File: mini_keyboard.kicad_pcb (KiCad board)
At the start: 2 copper layers, 61 x 53.3 mm, 2 parts, among them SW1 SW_DIP_x01, U1 ARDUINO_MICRO_SHIELD

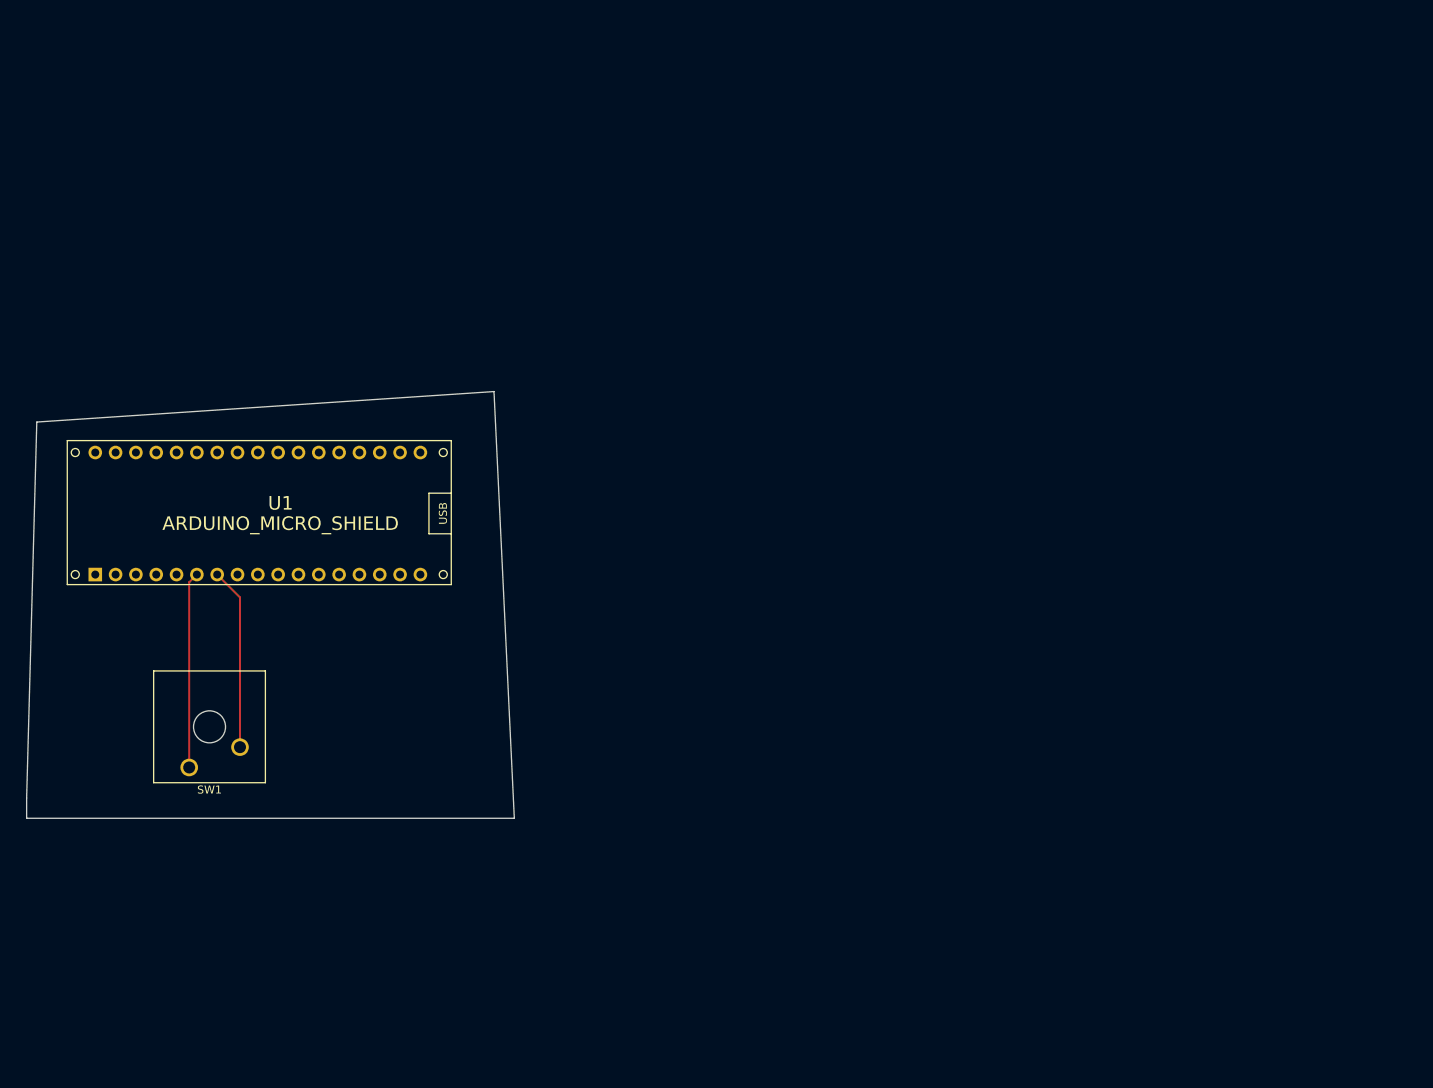
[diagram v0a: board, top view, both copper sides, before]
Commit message: PCB ready, no cables
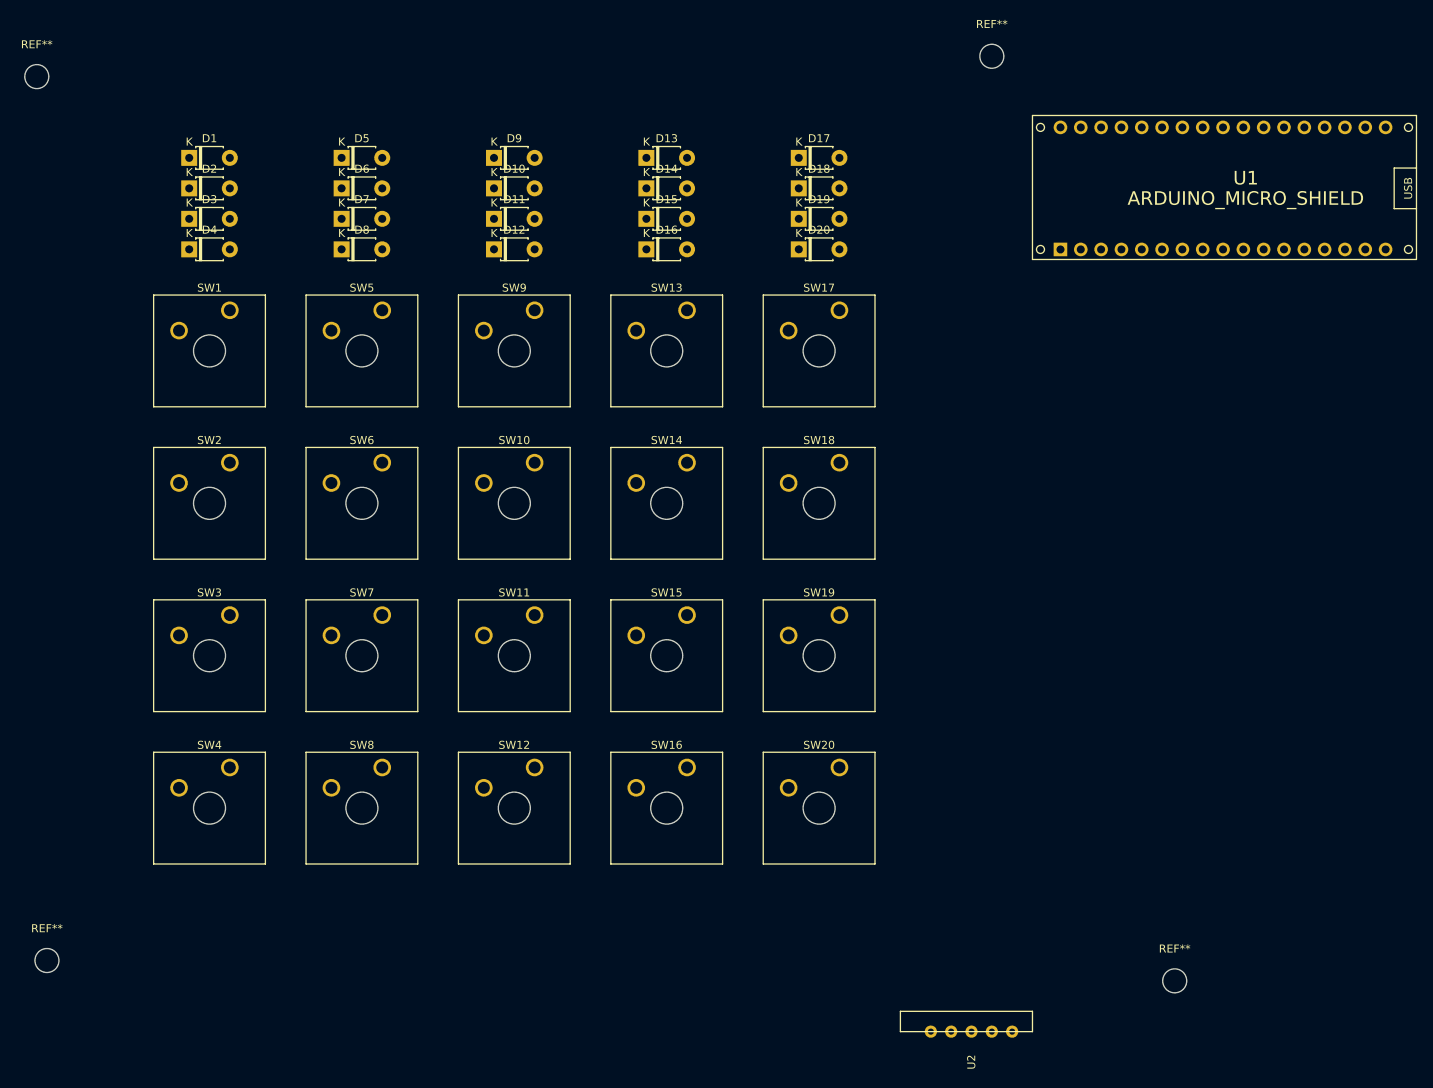
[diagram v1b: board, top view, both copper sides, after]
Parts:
- added D1: DIODE, Diode_THT:D_T-1_P5.08mm_Horizontal, F.Cu at (100.3, 33.0)
- added D10: DIODE, Diode_THT:D_T-1_P5.08mm_Horizontal, F.Cu at (138.4, 36.8)
- added D11: DIODE, Diode_THT:D_T-1_P5.08mm_Horizontal, F.Cu at (138.4, 40.6)
- added D12: DIODE, Diode_THT:D_T-1_P5.08mm_Horizontal, F.Cu at (138.4, 44.5)
- added D13: DIODE, Diode_THT:D_T-1_P5.08mm_Horizontal, F.Cu at (157.5, 33.0)
- added D14: DIODE, Diode_THT:D_T-1_P5.08mm_Horizontal, F.Cu at (157.5, 36.8)
- added D15: DIODE, Diode_THT:D_T-1_P5.08mm_Horizontal, F.Cu at (157.5, 40.6)
- added D16: DIODE, Diode_THT:D_T-1_P5.08mm_Horizontal, F.Cu at (157.5, 44.5)
- added D17: DIODE, Diode_THT:D_T-1_P5.08mm_Horizontal, F.Cu at (176.5, 33.0)
- added D18: DIODE, Diode_THT:D_T-1_P5.08mm_Horizontal, F.Cu at (176.5, 36.8)
- added D19: DIODE, Diode_THT:D_T-1_P5.08mm_Horizontal, F.Cu at (176.5, 40.6)
- added D2: DIODE, Diode_THT:D_T-1_P5.08mm_Horizontal, F.Cu at (100.3, 36.8)
- added D20: DIODE, Diode_THT:D_T-1_P5.08mm_Horizontal, F.Cu at (176.5, 44.5)
- added D3: DIODE, Diode_THT:D_T-1_P5.08mm_Horizontal, F.Cu at (100.3, 40.6)
- added D4: DIODE, Diode_THT:D_T-1_P5.08mm_Horizontal, F.Cu at (100.3, 44.5)
- added D5: DIODE, Diode_THT:D_T-1_P5.08mm_Horizontal, F.Cu at (119.4, 33.0)
- added D6: DIODE, Diode_THT:D_T-1_P5.08mm_Horizontal, F.Cu at (119.4, 36.8)
- added D7: DIODE, Diode_THT:D_T-1_P5.08mm_Horizontal, F.Cu at (119.4, 40.6)
- added D8: DIODE, Diode_THT:D_T-1_P5.08mm_Horizontal, F.Cu at (119.4, 44.5)
- added D9: DIODE, Diode_THT:D_T-1_P5.08mm_Horizontal, F.Cu at (138.4, 33.0)
- added REF**: MountingHole_3mm, MountingHole:MountingHole_3mm, F.Cu at (81.3, 22.9)
- added REF**: MountingHole_3mm, MountingHole:MountingHole_3mm, F.Cu at (200.7, 20.3)
- added REF**: MountingHole_3mm, MountingHole:MountingHole_3mm, F.Cu at (223.5, 135.9)
- added REF**: MountingHole_3mm, MountingHole:MountingHole_3mm, F.Cu at (82.5, 133.3)
- added SW10: SW_DIP_x01, Button_Switch_Keyboard:SW_Cherry_MX_1.00u_Plate, F.Cu at (143.5, 71.1)
- added SW11: SW_DIP_x01, Button_Switch_Keyboard:SW_Cherry_MX_1.00u_Plate, F.Cu at (143.5, 90.2)
- added SW12: SW_DIP_x01, Button_Switch_Keyboard:SW_Cherry_MX_1.00u_Plate, F.Cu at (143.5, 109.2)
- added SW13: SW_DIP_x01, Button_Switch_Keyboard:SW_Cherry_MX_1.00u_Plate, F.Cu at (162.6, 52.1)
- added SW14: SW_DIP_x01, Button_Switch_Keyboard:SW_Cherry_MX_1.00u_Plate, F.Cu at (162.6, 71.1)
- added SW15: SW_DIP_x01, Button_Switch_Keyboard:SW_Cherry_MX_1.00u_Plate, F.Cu at (162.6, 90.2)
- added SW16: SW_DIP_x01, Button_Switch_Keyboard:SW_Cherry_MX_1.00u_Plate, F.Cu at (162.6, 109.2)
- added SW17: SW_DIP_x01, Button_Switch_Keyboard:SW_Cherry_MX_1.00u_Plate, F.Cu at (181.6, 52.1)
- added SW18: SW_DIP_x01, Button_Switch_Keyboard:SW_Cherry_MX_1.00u_Plate, F.Cu at (181.6, 71.1)
- added SW19: SW_DIP_x01, Button_Switch_Keyboard:SW_Cherry_MX_1.00u_Plate, F.Cu at (181.6, 90.2)
- added SW2: SW_DIP_x01, Button_Switch_Keyboard:SW_Cherry_MX_1.00u_Plate, F.Cu at (105.4, 71.1)
- added SW20: SW_DIP_x01, Button_Switch_Keyboard:SW_Cherry_MX_1.00u_Plate, F.Cu at (181.6, 109.2)
- added SW3: SW_DIP_x01, Button_Switch_Keyboard:SW_Cherry_MX_1.00u_Plate, F.Cu at (105.4, 90.2)
- added SW4: SW_DIP_x01, Button_Switch_Keyboard:SW_Cherry_MX_1.00u_Plate, F.Cu at (105.4, 109.2)
- added SW5: SW_DIP_x01, Button_Switch_Keyboard:SW_Cherry_MX_1.00u_Plate, F.Cu at (124.5, 52.1)
- added SW6: SW_DIP_x01, Button_Switch_Keyboard:SW_Cherry_MX_1.00u_Plate, F.Cu at (124.5, 71.1)
- added SW7: SW_DIP_x01, Button_Switch_Keyboard:SW_Cherry_MX_1.00u_Plate, F.Cu at (124.5, 90.2)
- added SW8: SW_DIP_x01, Button_Switch_Keyboard:SW_Cherry_MX_1.00u_Plate, F.Cu at (124.5, 109.2)
- added SW9: SW_DIP_x01, Button_Switch_Keyboard:SW_Cherry_MX_1.00u_Plate, F.Cu at (143.5, 52.1)
- added U2: Joystick, Joystick:Joystick, F.Cu at (203.2, 142.2)
- moved U1 127.3 mm to (205.7, 45.7)
- moved SW1 57.4 mm to (105.4, 52.1), turned to 0 degrees
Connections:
- SW1 pad 1: Net-(SW1-Pad1) -> Net-(D1-Pad2)
- U1 pad 2: Net-(SW1-Pad2) -> Net-(D1-Pad1)
- U1 pad A5: Net-(U1-PadA5) -> Net-(SW1-Pad2)
- U1 pad GND: Net-(SW1-Pad1) -> Net-(U1-PadGND)
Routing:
- net Net-(SW1-Pad1): track 24.5 -> 0.00 mm
- net Net-(SW1-Pad2): track 22.8 -> 0.00 mm
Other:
- board outline removed

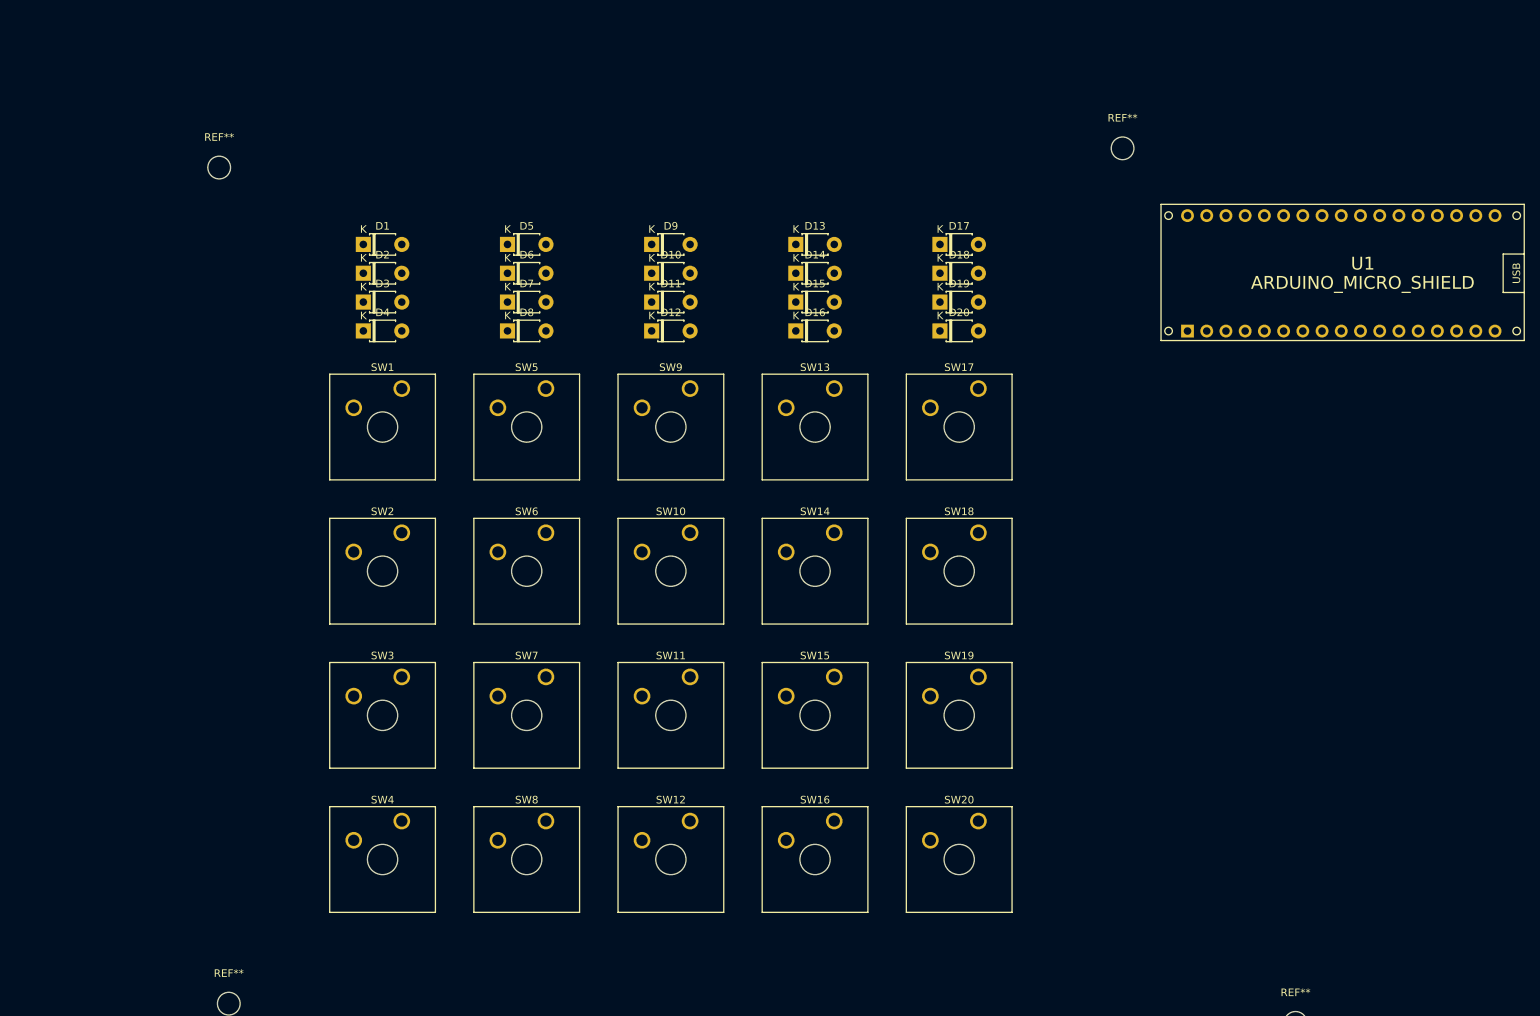
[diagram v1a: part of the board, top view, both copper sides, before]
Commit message: Moved buttons and made some lines
Problem: Some cables are crossing
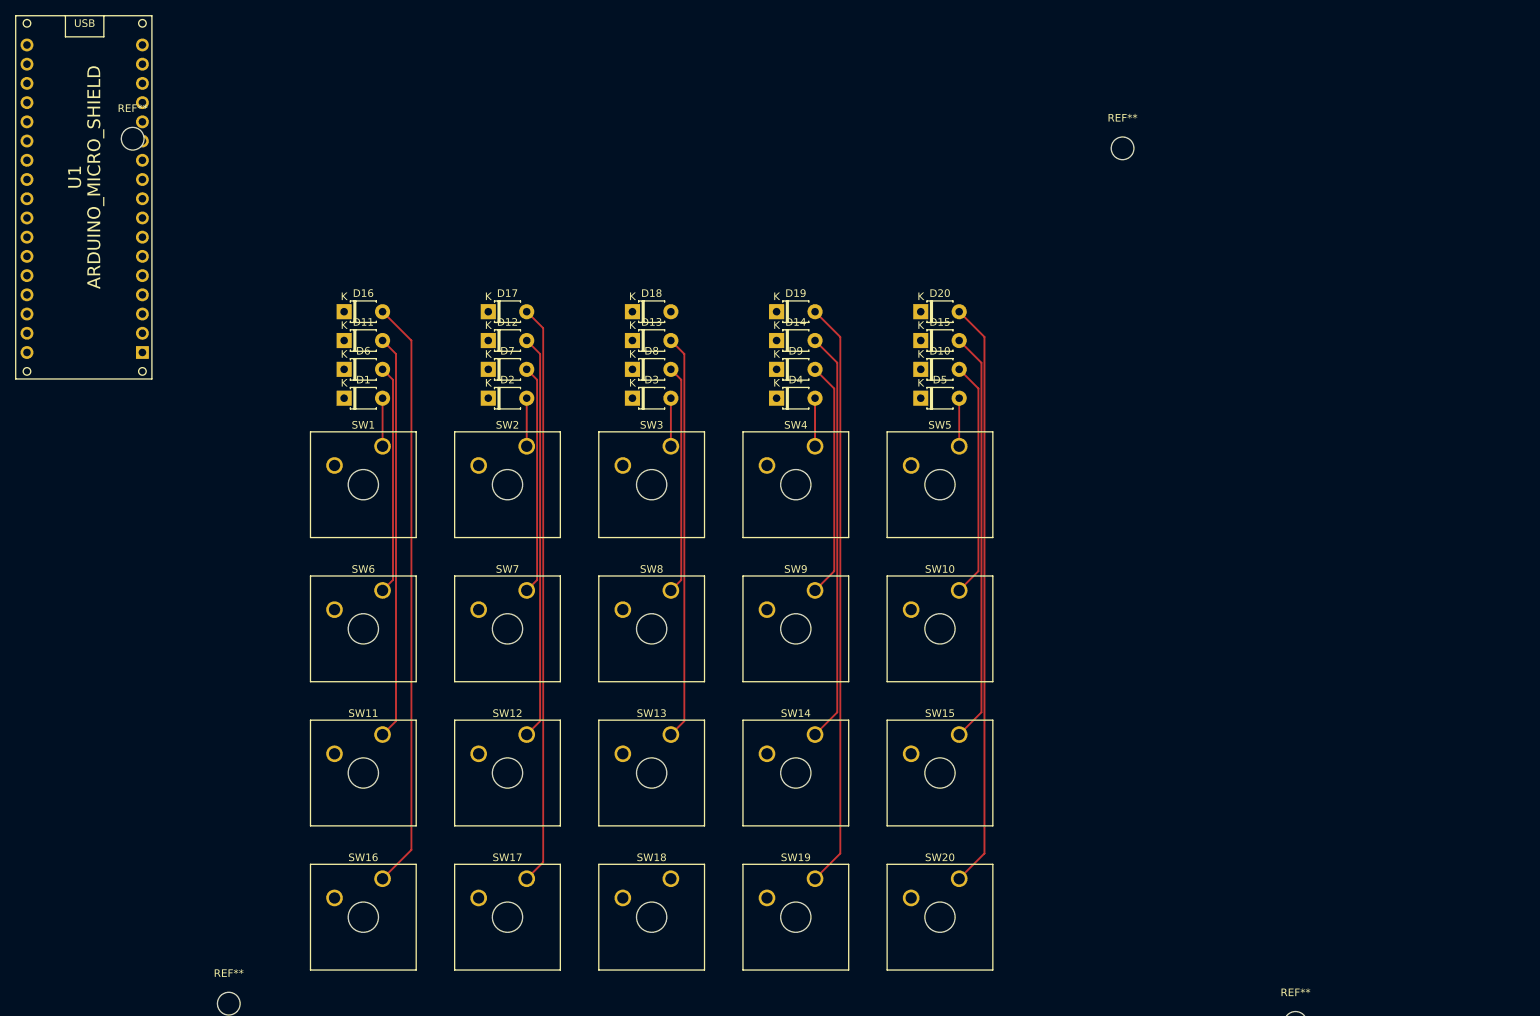
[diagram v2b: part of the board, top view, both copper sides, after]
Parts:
- moved U1 133.4 mm to (72.4, 50.8), turned to 90 degrees
- moved SW17 88.1 mm to (121.9, 116.8)
- moved SW4 73.7 mm to (160.0, 59.7)
- moved SW18 61.2 mm to (141.0, 116.8)
- moved D17 60.3 mm to (116.8, 41.9)
- moved SW16 60.2 mm to (102.9, 116.8)
- moved D16 59.7 mm to (97.8, 41.9)
- moved D5 58.3 mm to (174.0, 53.3)
- moved D4 55.3 mm to (154.9, 53.3)
- moved SW5 55.1 mm to (179.1, 59.7)
- moved SW13 50.6 mm to (141.0, 97.8)
- moved SW3 46.8 mm to (141.0, 59.7)
- moved SW11 41.3 mm to (102.9, 97.8)
- moved D18 41.0 mm to (135.9, 41.9)
- moved D11 41.0 mm to (97.8, 45.7)
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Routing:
- net Net-(D16-Pad2): track 0.00 -> 78.1 mm
- net Net-(D20-Pad2): track 0.00 -> 77.7 mm
- net Net-(D19-Pad2): track 0.00 -> 77.7 mm
- net Net-(D17-Pad2): track 0.00 -> 76.7 mm
- net Net-(D15-Pad2): track 0.00 -> 54.5 mm
- net Net-(D14-Pad2): track 0.00 -> 54.5 mm
- net Net-(D13-Pad2): track 0.00 -> 53.5 mm
- net Net-(D12-Pad2): track 0.00 -> 53.5 mm
- net Net-(D11-Pad2): track 0.00 -> 53.5 mm
- net Net-(D10-Pad2): track 0.00 -> 31.3 mm
- net Net-(D9-Pad2): track 0.00 -> 31.3 mm
- net Net-(D8-Pad2): track 0.00 -> 30.3 mm
- net Net-(D7-Pad2): track 0.00 -> 30.3 mm
- net Net-(D6-Pad2): track 0.00 -> 30.3 mm
- net Net-(D5-Pad2): track 0.00 -> 6.35 mm
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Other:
- net class Default: clearance 0.2 -> 0.15
- rule trace_clearance: 0.2 -> 0.15
